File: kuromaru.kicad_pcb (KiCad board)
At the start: 2 copper layers, 119.4 x 95.1 mm, 63 parts, among them J1 USB_C_Receptacle_USB2.0, J102 Serial, J5 Conn_01x02, SW1 SW_Push, SW2 SW_Push, U1 RP2040, U2 GD25Q80CEIGR, U3 XC6210B332MR-G, U4 25LCxxx, Y1 Crystal_GND24

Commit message: Before messing around with orientation
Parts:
- moved R5 0.55 mm to (143.9, 43.8)
- moved FB1 0.45 mm to (142.6, 43.4)
- moved R4 0.39 mm to (154.1, 42.0)
- moved J5 0.19 mm to (140.4, 43.6)
- moved SW2 0.17 mm to (140.4, 44.2)
- moved R3 0.12 mm to (140.5, 47.0)
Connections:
- C1R1 pad 2: Net-(C1R1-Pad2) -> Net-(C1R2-Pad4)
- C1R2 pad 2: Net-(C1R2-Pad2) -> Net-(C1R3-Pad4)
- C2R2 pad 2: Net-(C1R2-Pad4) -> Net-(C2R1-Pad4)
- C2R2 pad 4: Net-(C2R2-Pad4) -> Net-(C2R3-Pad2)
- C2R3 pad 2: Net-(C1R3-Pad4) -> Net-(C2R3-Pad2)
- C3R1 pad 2: Net-(C2R1-Pad4) -> Net-(C3R2-Pad4)
- C3R2 pad 2: Net-(C2R2-Pad4) -> Net-(C3R3-Pad4)
- C4R1 pad 4: Net-(C4R1-Pad4) -> Net-(C4R2-Pad2)
- C4R2 pad 2: Net-(C3R2-Pad4) -> Net-(C4R2-Pad2)
- C4R3 pad 2: Net-(C3R3-Pad4) -> Net-(C4R2-Pad4)
- C5R1 pad 2: Net-(C4R1-Pad4) -> Net-(C5R2-Pad4)
- C5R2 pad 2: Net-(C4R2-Pad4) -> Net-(C5R3-Pad4)
- C5R2 pad 4: Net-(C1R1-Pad2) -> Net-(C5R2-Pad4)
- C5R3 pad 4: Net-(C1R2-Pad2) -> Net-(C5R3-Pad4)
- U1 pad 11: switch_c3r2 -> switch_c2r2
- U1 pad 12: switch_c2r2 -> switch_c1r2
- U1 pad 13: switch_c1r2 -> switch_c5r2
- U1 pad 8: switch_c5r2 -> switch_c4r2
- U1 pad 9: switch_c4r2 -> switch_c3r2
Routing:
- net +3V3: track 174.6 -> 494.6 mm, vias 6 -> 19
- net switch_c5r3: track 53.7 -> 129.0 mm
- net switch_c5r2: track 43.4 -> 110.5 mm
- net switch_c5r1: track 43.4 -> 100.7 mm, vias 0 -> 1
- net switch_c4r2: track 43.4 -> 84.6 mm
- net Net-(C2R3-Pad2): track 0.00 -> 40.8 mm, vias 0 -> 2
- net Net-(C4R2-Pad2): track 0.00 -> 40.5 mm
- net switch_c4r1: track 43.5 -> 83.8 mm, vias 0 -> 1
- net switch_c4r3: track 56.1 -> 95.4 mm
- net Net-(C1R3-Pad2): track 0.00 -> 37.9 mm
- net Net-(C4R3-Pad4): track 0.00 -> 27.0 mm
- net Net-(C1R3-Pad4): track 14.0 -> 37.3 mm, vias 0 -> 2
- net switch_c3r1: track 43.4 -> 65.7 mm, vias 0 -> 1
- net Net-(C5R3-Pad4): track 0.00 -> 21.5 mm
- net Net-(C5R2-Pad4): track 0.00 -> 20.9 mm
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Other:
- board size 119.4 x 95.1 mm -> 125.5 x 95.1 mm

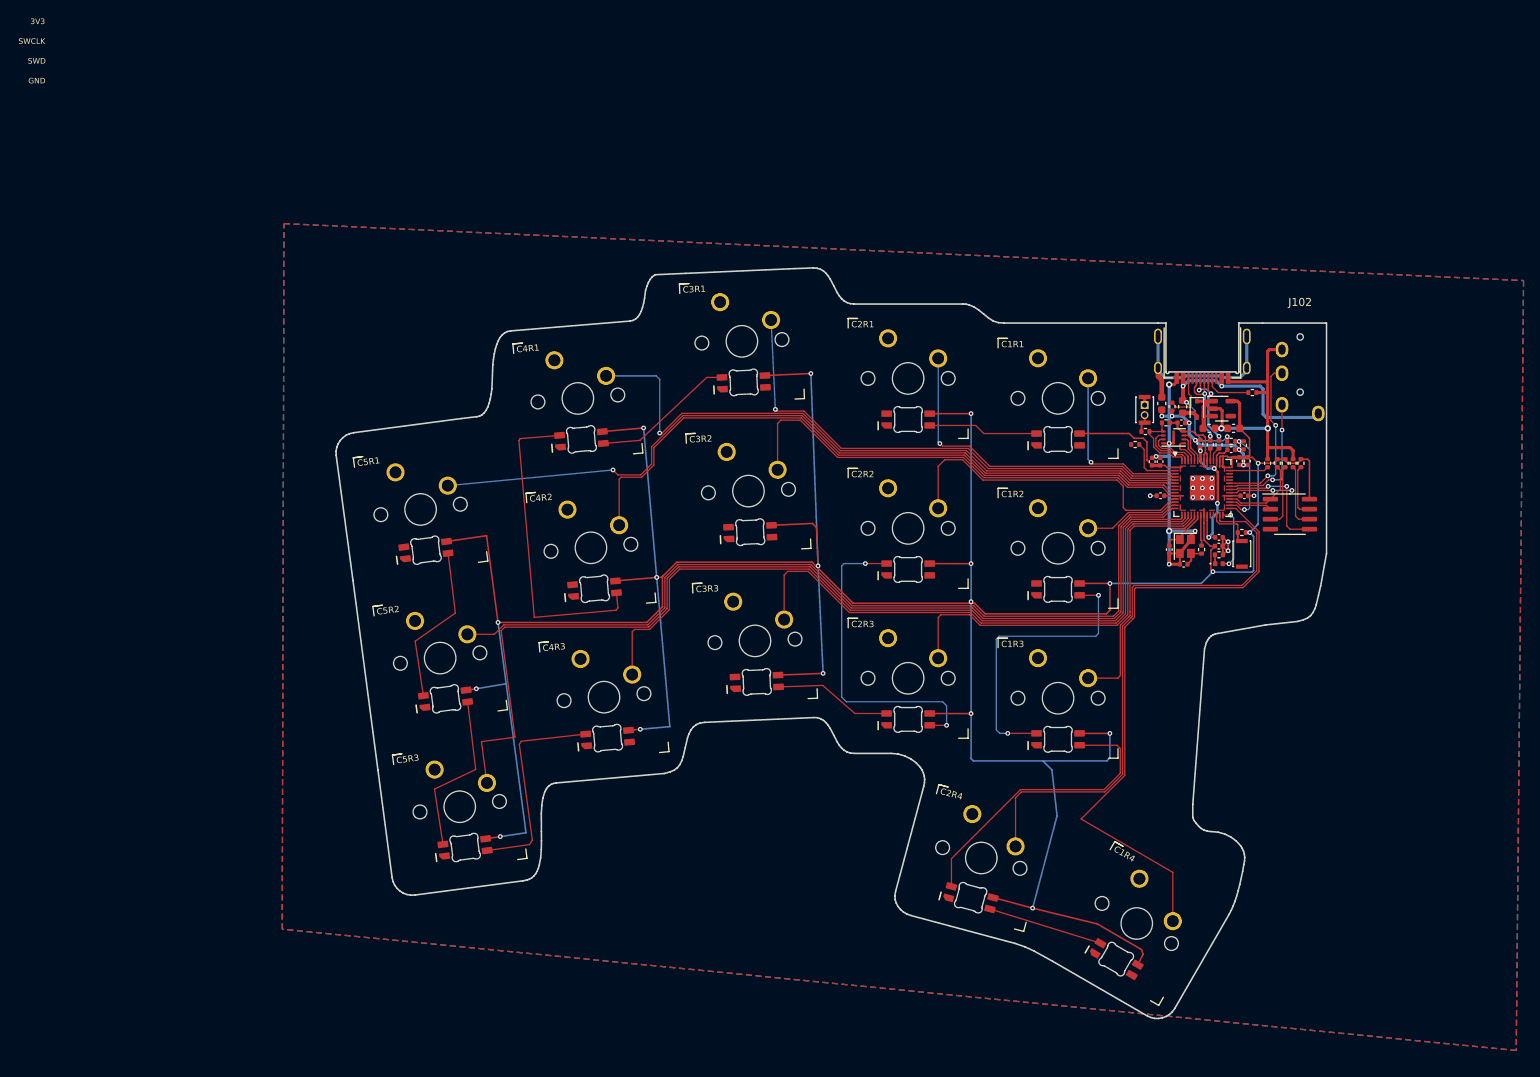
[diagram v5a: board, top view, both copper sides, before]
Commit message: Some reroute with better orientation
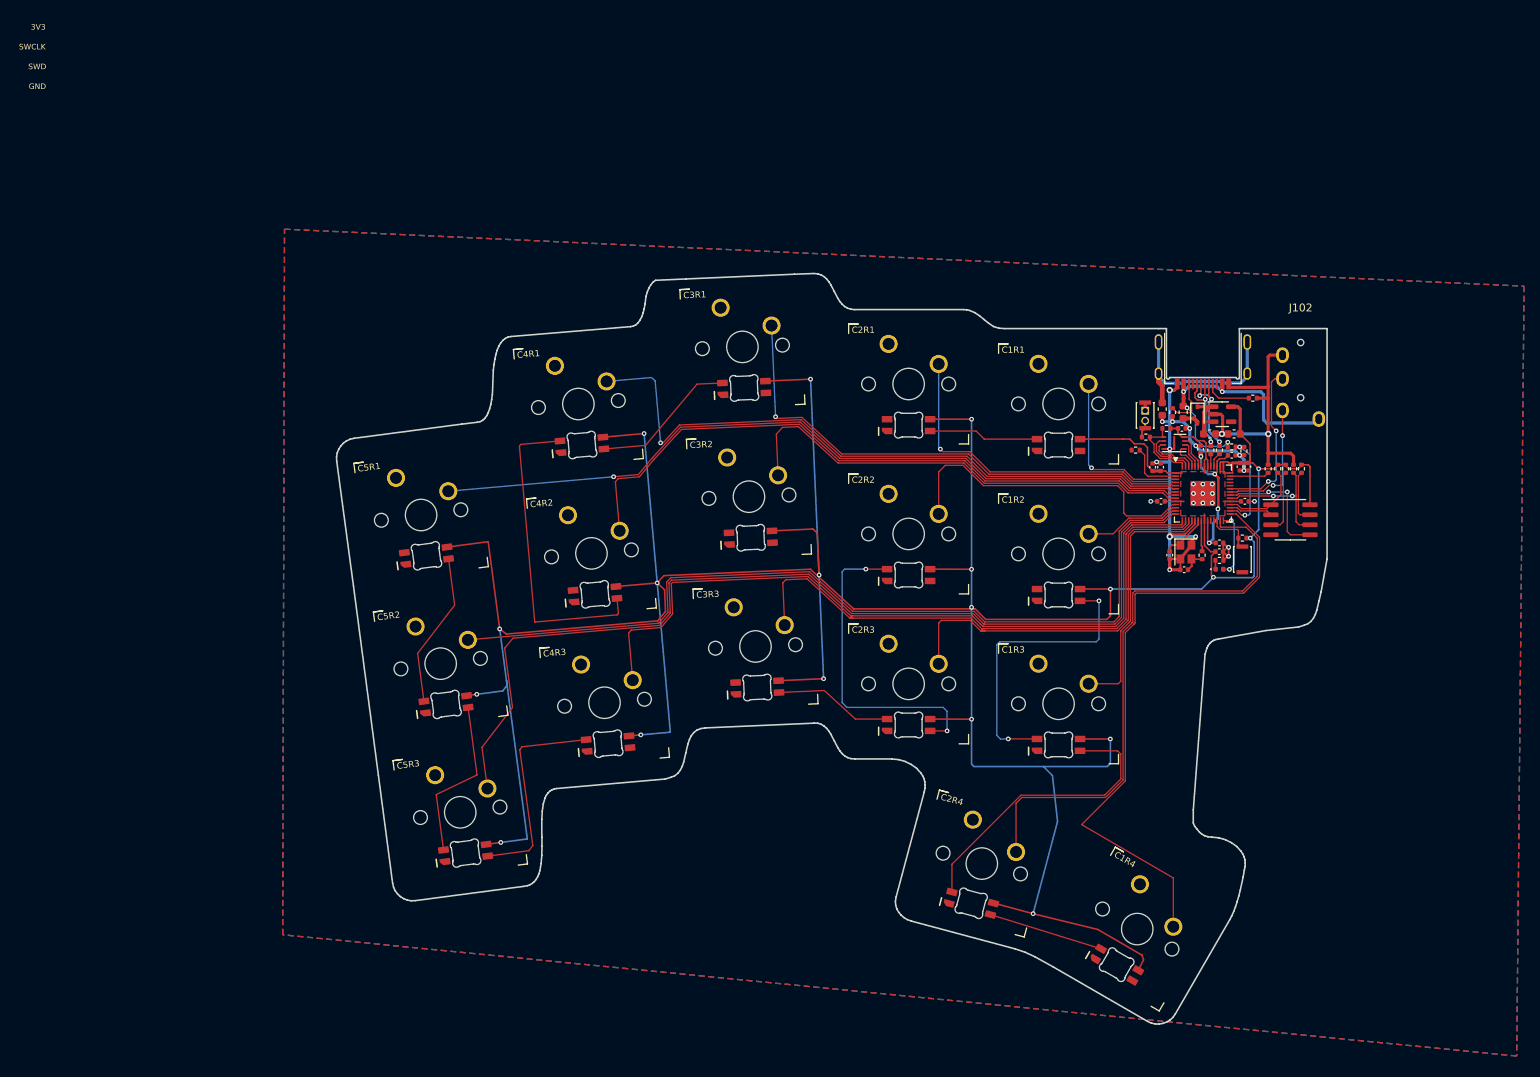
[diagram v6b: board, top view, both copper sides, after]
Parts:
- moved R6 0.71 mm to (148.8, 49.3)
- moved C2R1 0.71 mm to (110.5, 40.9)
- moved C2 0.71 mm to (151.7, 47.3)
- moved D1 0.71 mm to (149.9, 64.4)
- moved C12 0.71 mm to (142.4, 51.5)
- moved C11 0.71 mm to (152.5, 51.4)
- moved C3R3 0.71 mm to (91.1, 74.2)
- moved C2R2 0.71 mm to (110.5, 59.9)
- moved C10 0.71 mm to (145.1, 46.6)
- moved R9 0.71 mm to (143.2, 46.6)
- moved J1 0.71 mm to (147.8, 33.5)
- moved J5 0.71 mm to (140.5, 44.3)
- moved C4R2 0.71 mm to (70.3, 62.4)
- moved F1 0.71 mm to (145.3, 44.5)
- moved J102 0.71 mm to (160.2, 39.1)
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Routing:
- net switch_c5r3: track 129.0 -> 124.4 mm
- net switch_c5r1: track 100.7 -> 98.6 mm
- net +3V3: track 494.6 -> 495.8 mm
- net switch_c5r2: track 110.5 -> 109.4 mm
- net Net-(C5R2-Pad4): track 20.9 -> 19.8 mm
- net switch_c4r2: track 84.6 -> 83.8 mm

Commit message: Fix a few violations
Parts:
- moved C6 0.62 mm to (151.5, 50.6)
- moved C1R4 0.62 mm to (139.5, 110.6)
- moved C2R4 0.62 mm to (119.8, 102.3)
- moved C3R3 0.62 mm to (91.1, 74.8)
- moved C5R3 0.62 mm to (53.7, 95.8)
- moved C11 0.62 mm to (152.5, 52.0)
- moved C5 0.62 mm to (153.5, 52.0)
- moved R5 0.62 mm to (144.0, 45.1)
- moved R9 0.62 mm to (143.2, 47.2)
- moved C2 0.62 mm to (151.8, 47.9)
- moved R15 0.62 mm to (139.3, 49.9)
- moved C3R2 0.62 mm to (90.3, 55.8)
- moved C4R3 0.62 mm to (72.0, 81.9)
- moved J1 0.62 mm to (147.8, 34.1)
- moved C12 0.62 mm to (142.4, 52.1)
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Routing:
- net switch_c4r1: track 84.0 -> 88.8 mm
